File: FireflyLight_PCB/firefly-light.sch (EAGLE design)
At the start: 17 parts, among them IC1 TINY22P, IC2 TINY22P, Q1 BSS123, Q2 BSS123, Q3 BSS123

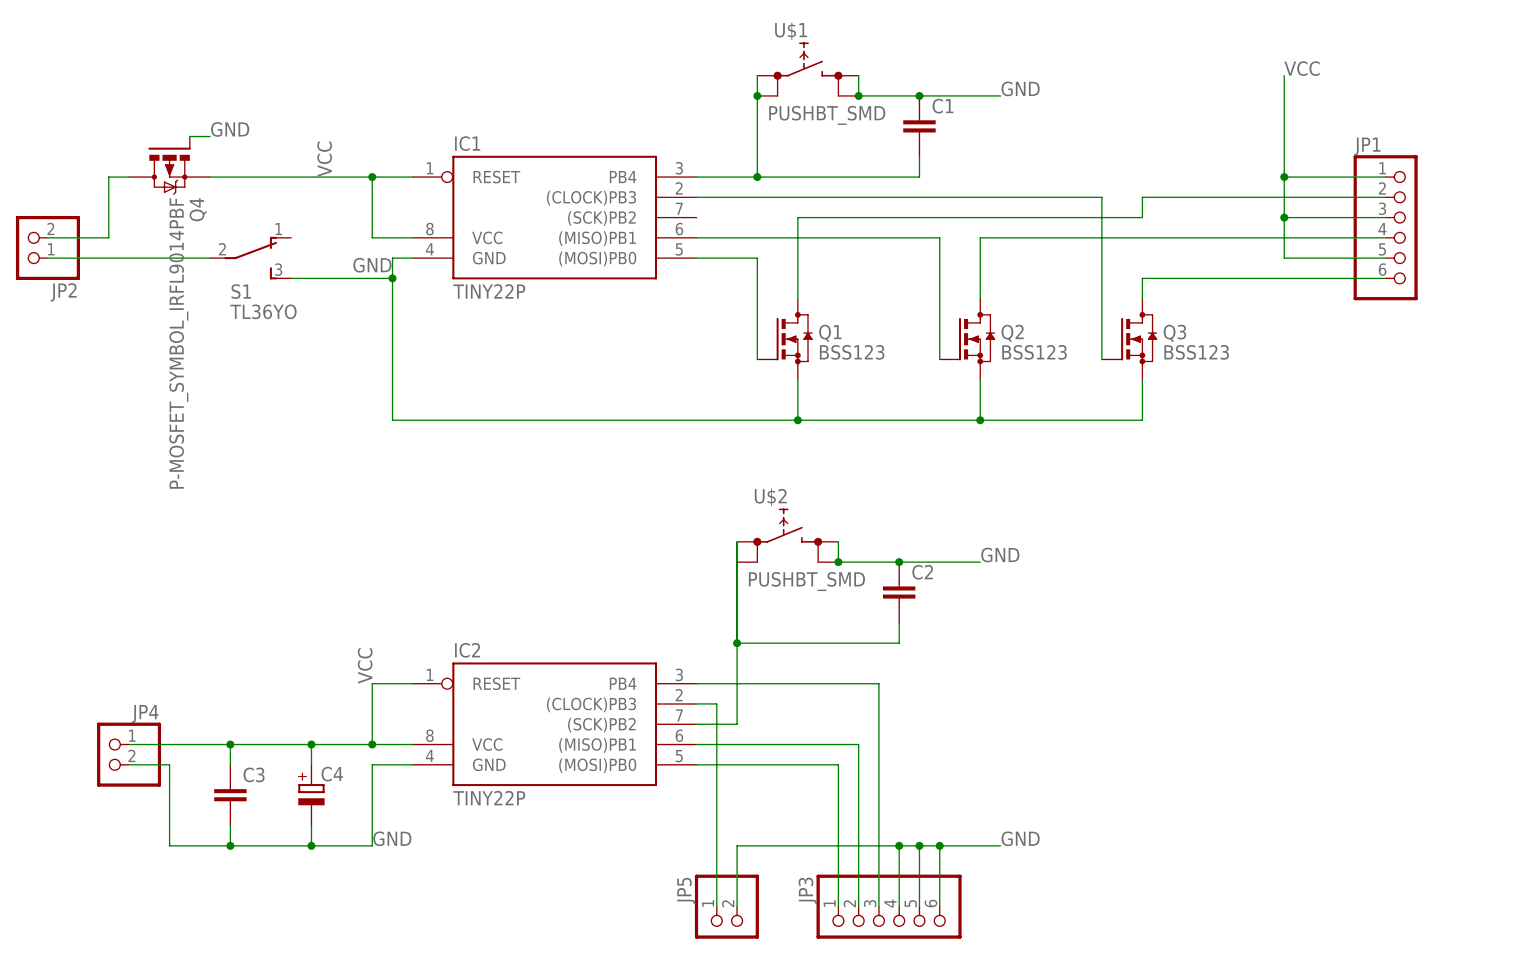
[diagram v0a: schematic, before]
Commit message: removed alternative schematic, edited for blog export
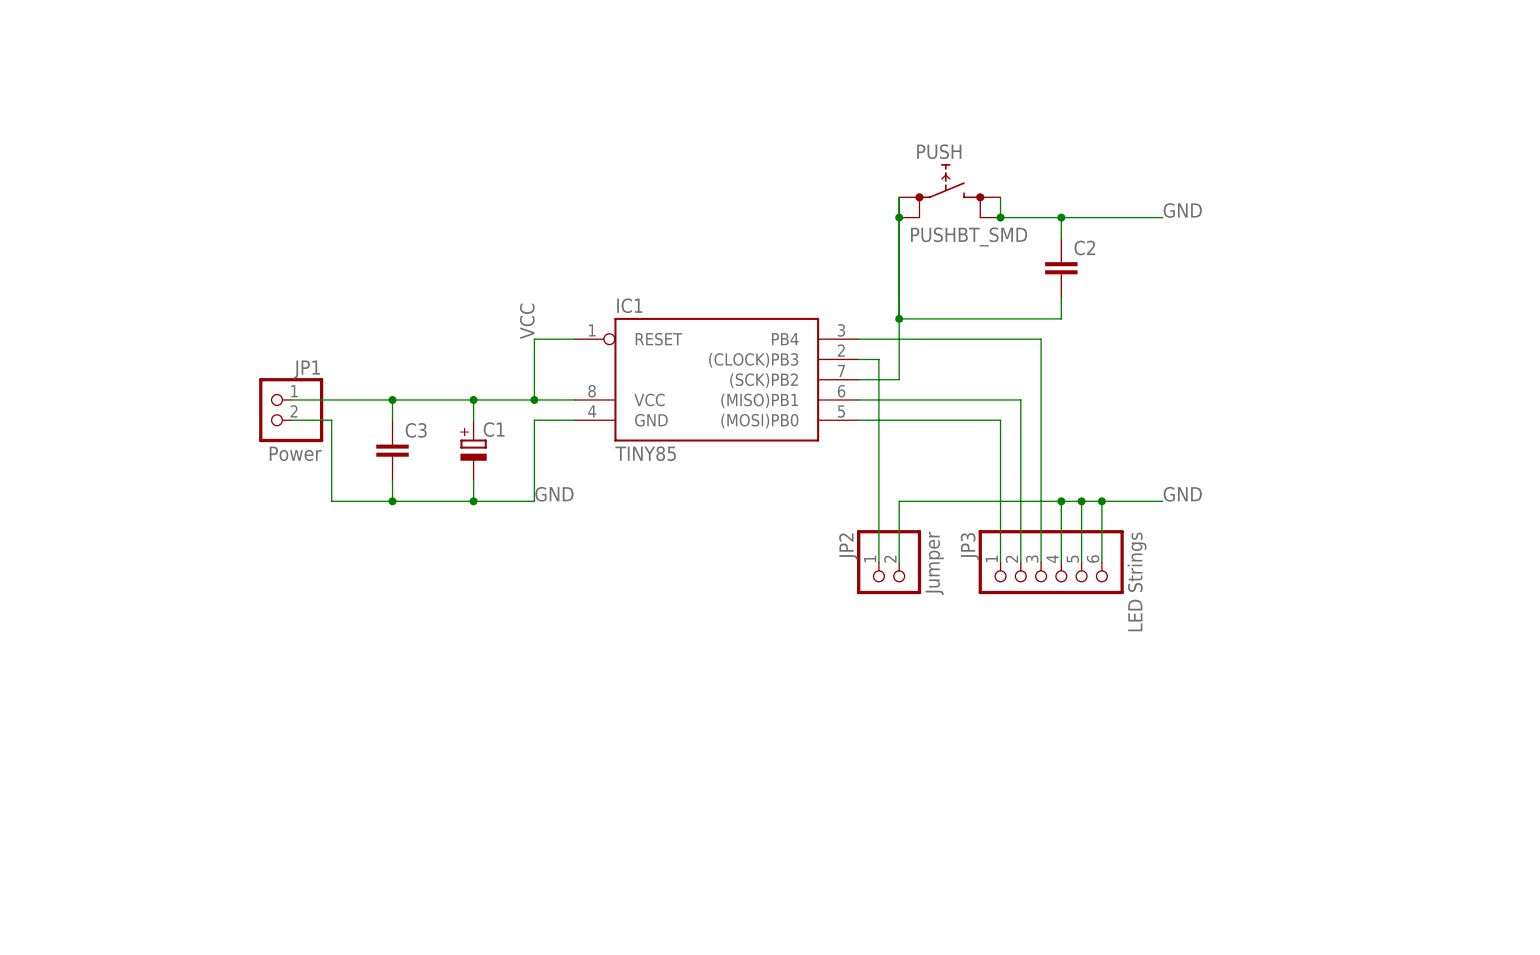
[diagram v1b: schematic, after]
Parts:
- removed C4: (no value), rcl:CPOL-EU140CLH-0810
- removed IC2: TINY22P, atmel:TINY22P
- removed JP4, JP5: (no value), pinhead:PINHD-1X2
- removed Q1, Q2, Q3: BSS123, transistor-small-signal:BSS123
- removed S1: TL36YO, switch:TL36YO
- removed U$1, U$2: PUSHBT_SMD, shyd:PUSHBT_SMD
- added PUSH: PUSHBT_SMD, shyd:PUSHBT_SMD
- C1: device rcl:C-EUC0805 -> rcl:CPOL-EU140CLH-0810
- IC1: value TINY22P -> TINY85
- JP1: value (none) -> Power; device pinhead:PINHD-1X6 -> pinhead:PINHD-1X2
- JP2: value (none) -> Jumper
- JP3: value (none) -> LED Strings
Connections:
- removed net N$1: IC1.(MOSI)PB0, Q1.G
- removed net N$2: IC1.(MISO)PB1, Q2.G
- removed net N$3: IC1.(CLOCK)PB3, Q3.G
- removed net N$4: C1.2, IC1.PB4, U$1.0@A, U$1.0@B
- removed net N$5: JP1.6, Q3.D
- removed net N$6: JP1.4, Q2.D
- removed net N$7: JP1.2, Q1.D
- removed net N$8: JP2.1, S1.P
- removed net N$9: JP2.2
- net GND: now also C1.-, JP1.2, JP2.2, PUSH.1@A, PUSH.1@B; no longer C1.1, C4.-, IC2.GND, JP4.2, JP5.2, Q1.S, Q2.S, Q3.S, S1.S, U$1.1@A, U$1.1@B, U$2.1@A, U$2.1@B
- net N$10: now also IC1.(MOSI)PB0; no longer IC2.(MOSI)PB0
- net N$11: now also IC1.(MISO)PB1; no longer IC2.(MISO)PB1
- net N$12: now also IC1.PB4; no longer IC2.PB4
- net N$16: now also IC1.(SCK)PB2, PUSH.0@A, PUSH.0@B; no longer IC2.(SCK)PB2, U$2.0@A, U$2.0@B
- net N$18: now also IC1.(CLOCK)PB3, JP2.1; no longer IC2.(CLOCK)PB3, JP5.1
- net VCC: now also C1.+; no longer C4.+, IC2.RESET, IC2.VCC, JP1.3, JP1.5, JP4.1
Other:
- moved on the sheet: C2, C3, IC1, JP2, JP3

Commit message: added missing values
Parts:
- C1: value (none) -> 330u
- C2, C3: value (none) -> 100n
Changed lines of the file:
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@@
 <part name="JP3" library="pinhead" deviceset="PINHD-1X6" device="" value="LED Strings"/>
 <part name="PUSH" library="shyd" deviceset="PUSHBT" device="_SMD"/>
-<part name="C2" library="rcl" deviceset="C-EU" device="C0805"/>
+<part name="C2" library="rcl" deviceset="C-EU" device="C0805" value="100n"/>
 <part name="JP1" library="pinhead" deviceset="PINHD-1X2" device="" value="Power"/>
 <part name="JP2" library="pinhead" deviceset="PINHD-1X2" device="" value="Jumper"/>
-<part name="C3" library="rcl" deviceset="C-EU" device="C0805"/>
-<part name="C1" library="rcl" deviceset="CPOL-EU" device="140CLH-0810"/>
+<part name="C3" library="rcl" deviceset="C-EU" device="C0805" value="100n"/>
+<part name="C1" library="rcl" deviceset="CPOL-EU" device="140CLH-0810" value="330u"/>
 </parts>
 <sheets>

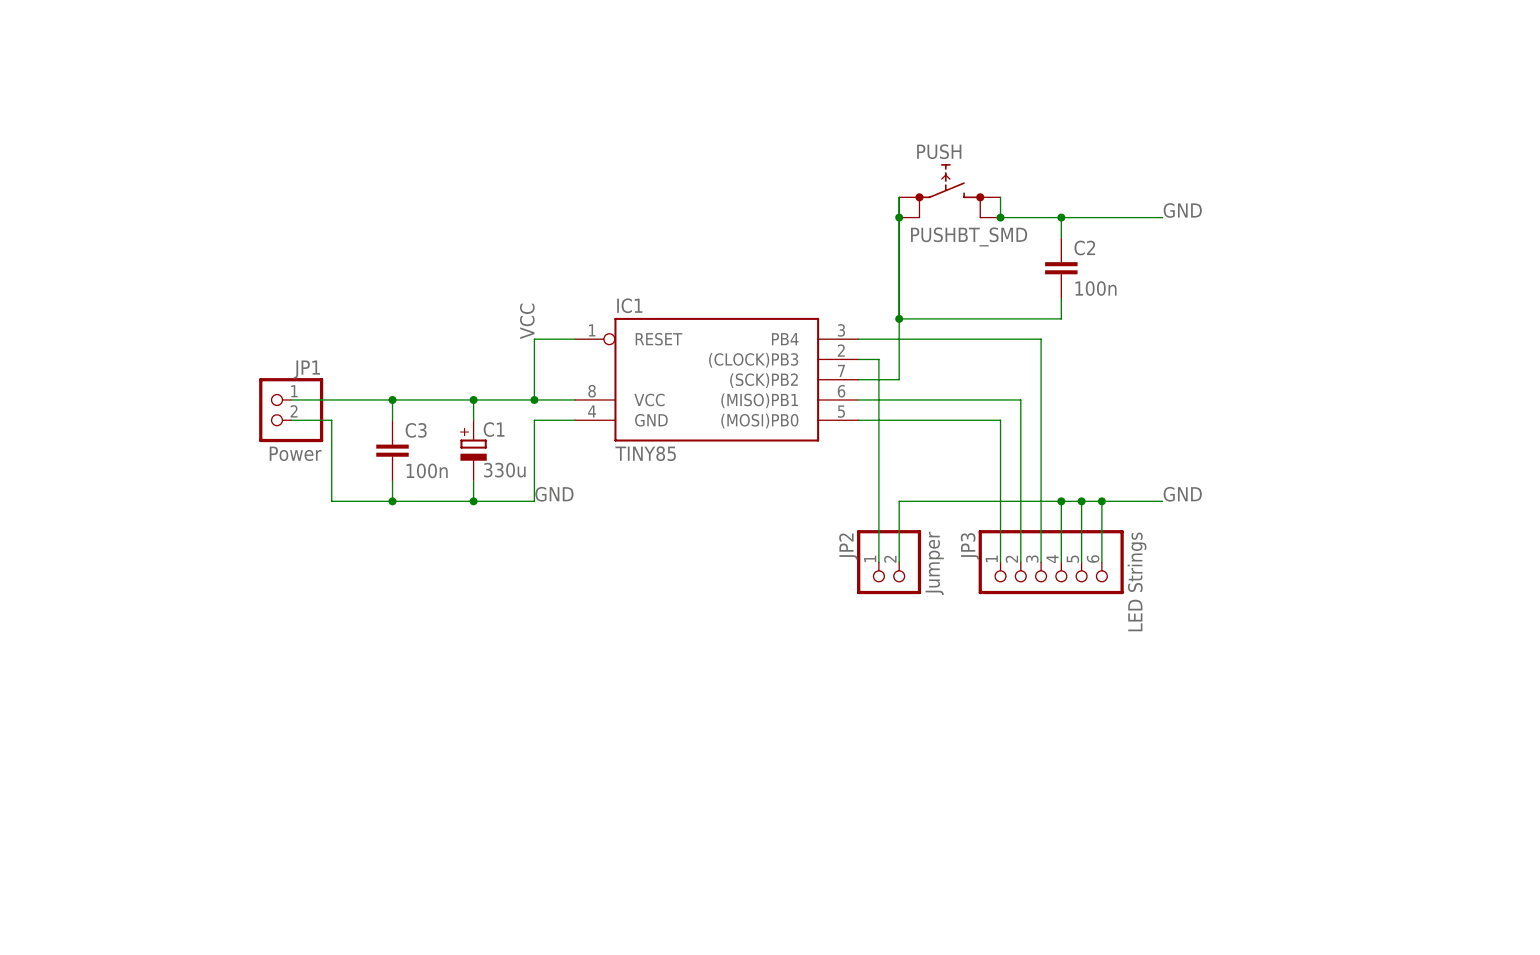
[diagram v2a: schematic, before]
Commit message: added mosfets and ISP
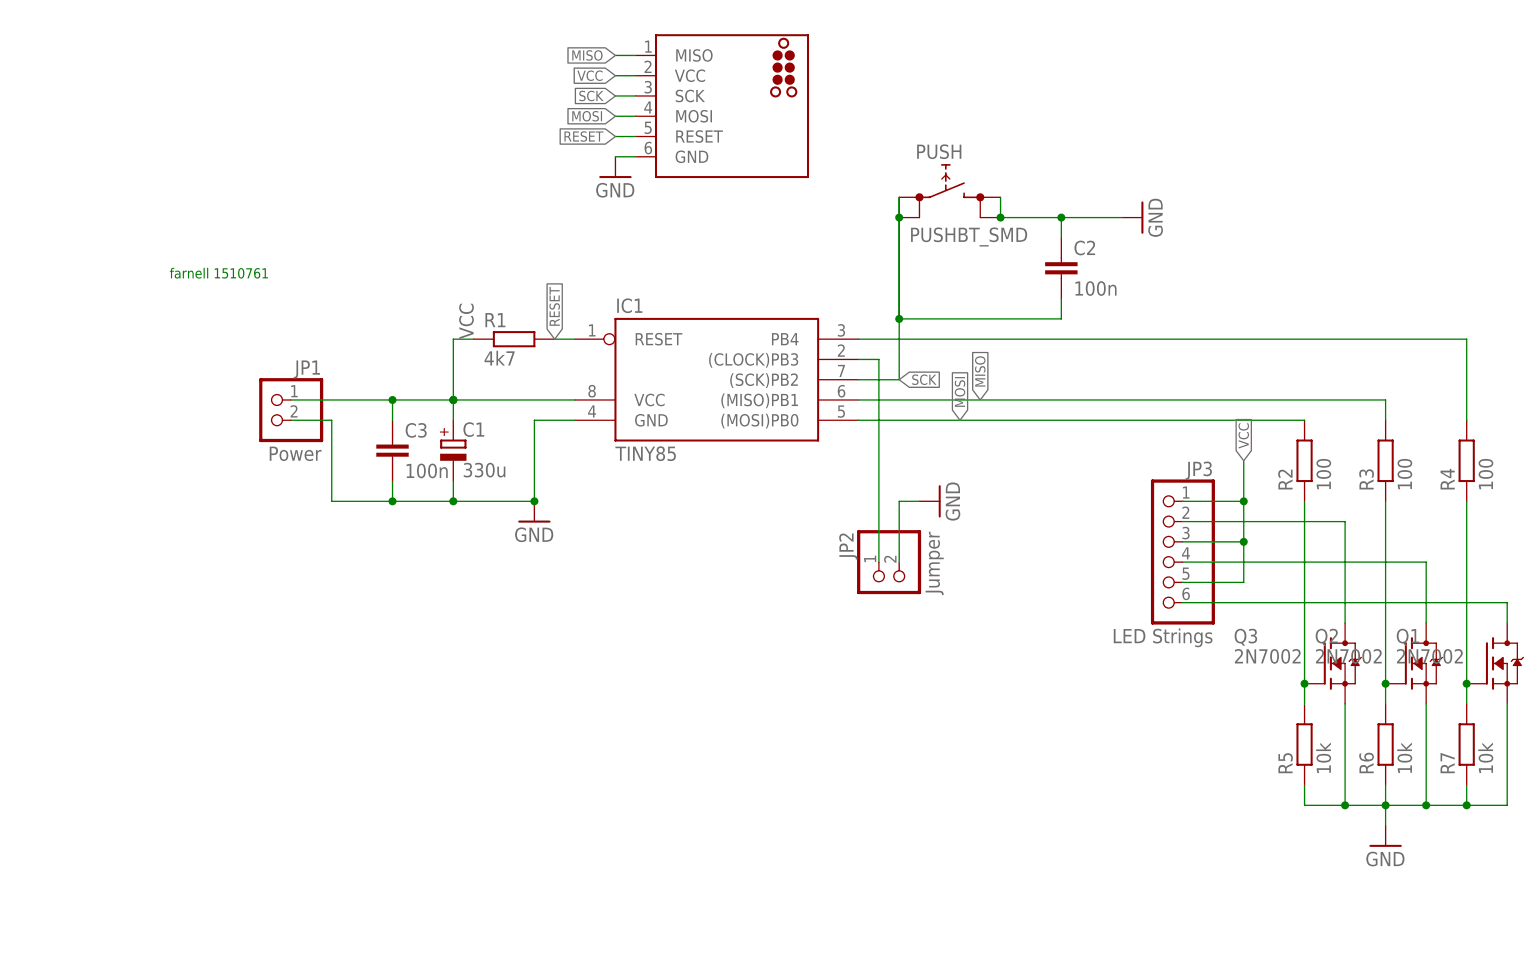
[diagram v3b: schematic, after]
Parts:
- added Q1, Q2, Q3: 2N7002, Meine:2N7002
- added R1: 4k7, rcl:R-EU_R0805
- added R2, R3, R4: 100, rcl:R-EU_R0805
- added R5, R6, R7: 10k, rcl:R-EU_R0805
- added U$1: TC2030-MCP-NL, Meine:TC2030-MCP-NL
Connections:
- removed net N$10: IC1.(MOSI)PB0, JP3.1
- removed net N$11: IC1.(MISO)PB1, JP3.2
- removed net N$16: C2.2, IC1.(SCK)PB2, PUSH.0@A, PUSH.0@B
- new net MISO: IC1.(MISO)PB1, R3.2, U$1.MISO
- new net MOSI: IC1.(MOSI)PB0, R2.2, U$1.MOSI
- new net N$1: Q3.G, R2.1, R5.2
- new net N$2: Q2.G, R3.1, R6.2
- new net N$3: Q1.G, R4.1, R7.2
- new net N$5: JP3.2, Q3.D
- new net N$6: JP3.4, Q2.D
- new net N$7: JP3.6, Q1.D
- new net RESET: IC1.RESET, R1.2, U$1.RESET
- new net SCK: C2.2, IC1.(SCK)PB2, PUSH.0@A, PUSH.0@B, U$1.SCK
- net GND: now also Q1.S, Q2.S, Q3.S, R5.1, R6.1, R7.1, U$1.GND; no longer JP3.4, JP3.5, JP3.6
- net N$12: now also R4.2; no longer JP3.3
- net VCC: now also JP3.1, JP3.3, JP3.5, R1.1, U$1.VCC; no longer IC1.RESET
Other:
- note added: "farnell 1510761"
- moved on the sheet: C1, JP3

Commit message: added pcb layout
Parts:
- C1: device rcl:CPOL-EU140CLH-0810 -> rcl:CPOL-EUE3.5-8
- renumbered PUSH to NEXT, U$1 to ISP
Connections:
- net N$1: now also Q1.G; no longer Q3.G
- net N$3: now also Q3.G; no longer Q1.G
- net N$5: now also Q1.D; no longer Q3.D
- net N$7: now also Q3.D; no longer Q1.D
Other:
- moved on the sheet: Q1, Q3

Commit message: attiny is now SO8
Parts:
- IC1: device atmel:TINY22P -> atmel:TINY22S
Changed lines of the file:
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@@
 </classes>
 <parts>
-<part name="IC1" library="atmel" library_urn="urn:adsk.eagle:library:105" deviceset="TINY22" device="P" package3d_urn="urn:adsk.eagle:package:4324/1" value="TINY85"/>
+<part name="IC1" library="atmel" library_urn="urn:adsk.eagle:library:105" deviceset="TINY22" device="S" package3d_urn="urn:adsk.eagle:package:4326/1" value="TINY85"/>
 <part name="JP3" library="pinhead" library_urn="urn:adsk.eagle:library:325" deviceset="PINHD-1X6" device="" package3d_urn="urn:adsk.eagle:package:22472/2" value="LED Strings"/>
 <part name="NEXT" library="shyd" deviceset="PUSHBT" device="_SMD"/>
